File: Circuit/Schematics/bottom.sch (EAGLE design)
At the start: 42 parts, among them IC1 LM2936MP-3.3, X2 16 Mhz, X3 16 Mhz

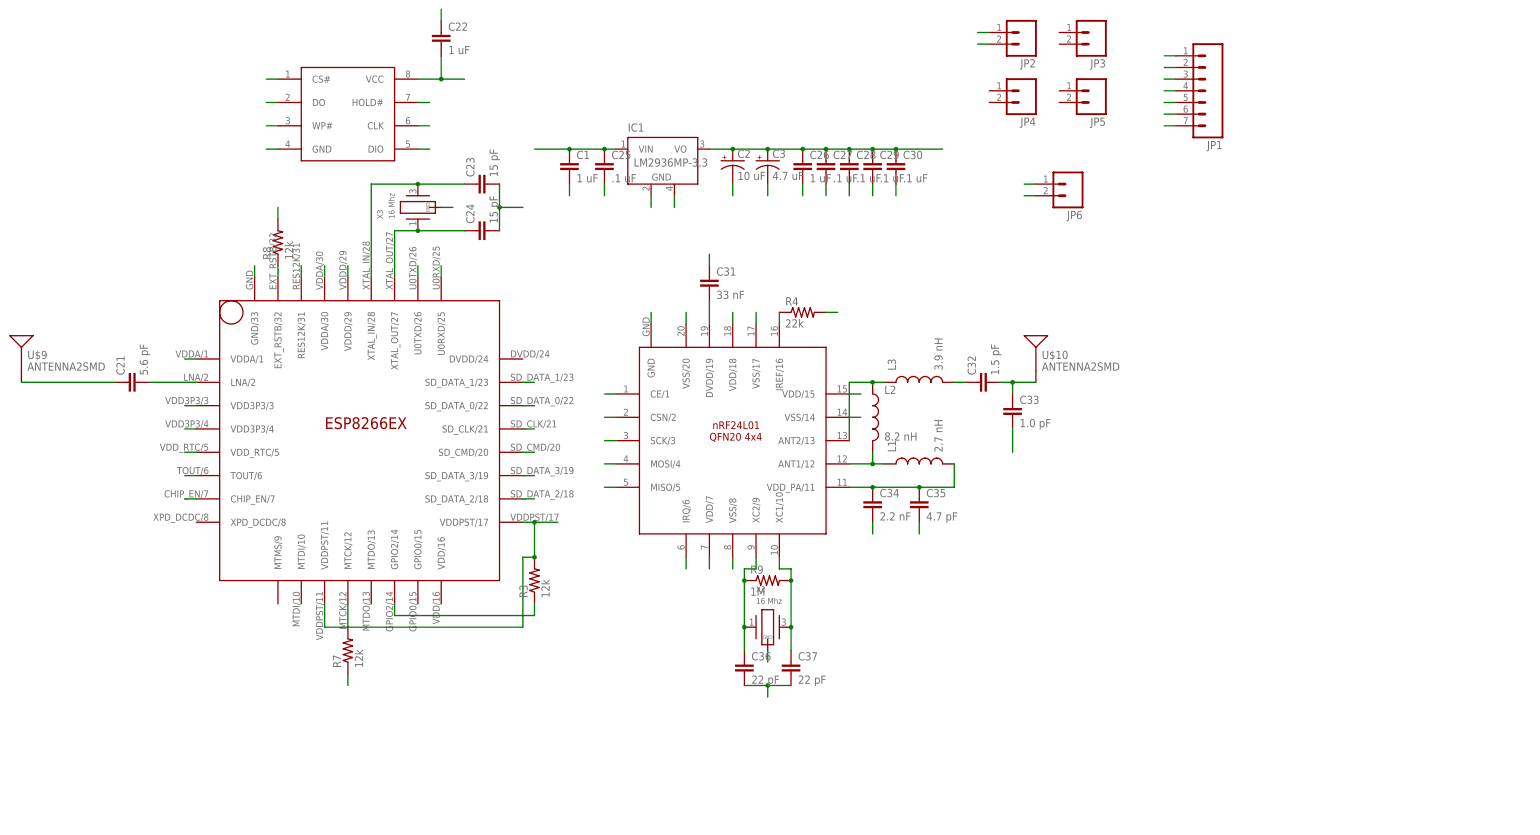
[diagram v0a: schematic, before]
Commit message: P1 preliminary boards finished
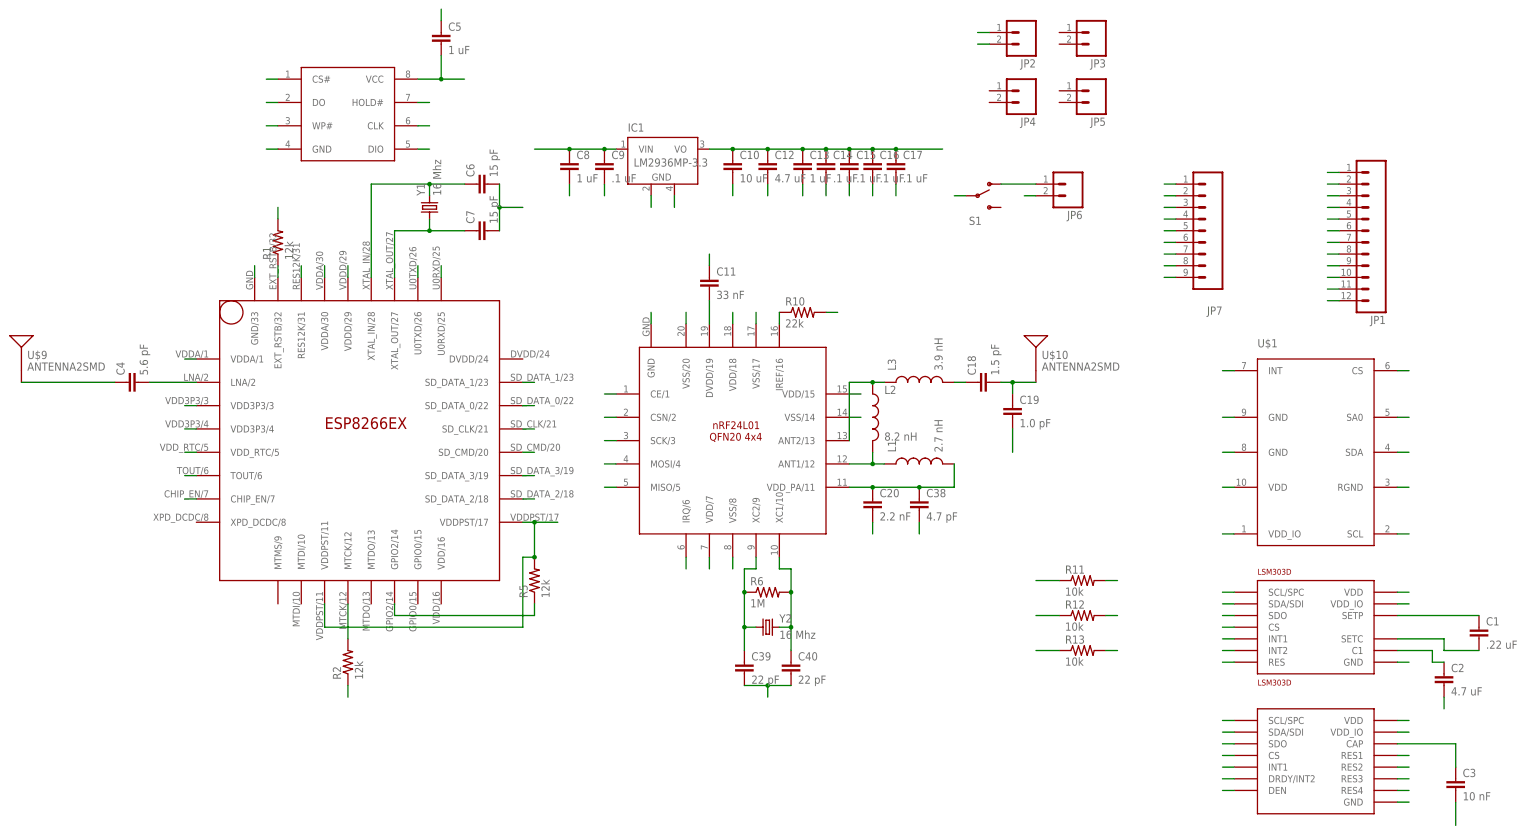
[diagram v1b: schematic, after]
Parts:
- removed C21: 5.6 pF, SparkFun-Capacitors:CAP0402-CAP
- removed C22, C26: 1 uF, SparkFun-Capacitors:CAP0402-CAP
- removed C23, C24: 15 pF, SparkFun-Capacitors:CAP0402-CAP
- removed C25, C27, C28, C29, C30: .1 uF, SparkFun-Capacitors:CAP0402-CAP
- removed C31: 33 nF, SparkFun-Capacitors:CAP0402-CAP
- removed C32: 1.5 pF, SparkFun-Capacitors:CAP0402-CAP
- removed C33: 1.0 pF, SparkFun-Capacitors:CAP0402-CAP
- removed C34: 2.2 nF, SparkFun-Capacitors:CAP0402-CAP
- removed C35: 4.7 pF, SparkFun-Capacitors:CAP0402-CAP
- removed C36, C37: 22 pF, SparkFun-Capacitors:CAP0402-CAP
- removed R3, R7, R8: 12k, SparkFun-Resistors:RESISTOR0402
- removed R4: 22k, SparkFun-Resistors:RESISTOR0402
- removed R9: 1M, SparkFun-Resistors:RESISTOR0402
- removed X2, X3: 16 Mhz, crystals:TXC-8Y
- added C10: 10 uF, SparkFun-Capacitors:CAP0603-CAP
- added C11: 33 nF, SparkFun-Capacitors:CAP0603-CAP
- added C12: 4.7 uF, SparkFun-Capacitors:CAP0603-CAP
- added C13, C5, C8: 1 uF, SparkFun-Capacitors:CAP0603-CAP
- added C14, C15, C16, C17, C9: .1 uF, SparkFun-Capacitors:CAP0603-CAP
- added C18: 1.5 pF, SparkFun-Capacitors:CAP0603-CAP
- added C19: 1.0 pF, SparkFun-Capacitors:CAP0603-CAP
- added C20: 2.2 nF, SparkFun-Capacitors:CAP0603-CAP
- added C38: 4.7 pF, SparkFun-Capacitors:CAP0603-CAP
- added C39, C40: 22 pF, SparkFun-Capacitors:CAP0603-CAP
- added C4: 5.6 pF, SparkFun-Capacitors:CAP0603-CAP
- added C6, C7: 15 pF, SparkFun-Capacitors:CAP0603-CAP
- added JP7: (no value), SparkFun-Connectors:M09
- added L3GD20H: L3GD20H, st:L3GD20H
- added LSM303D: LSM303D, st:LSM303D
- added R1, R2, R5: 12k, SparkFun-Resistors:RESISTOR0603-RES
- added R10: 22k, SparkFun-Resistors:RESISTOR0603-RES
- added R11, R12, R13: 10k, SparkFun-Resistors:RESISTOR0603-RES
- added R6: 1M, SparkFun-Resistors:RESISTOR0603-RES
- added S1: (no value), SparkFun-Electromechanical:SWITCH-SPDT-SMD-A
- added U$1: LPS25H, chips:LPS25H
- added Y1, Y2: 16 Mhz, SparkFun-FreqCtrl:CRYSTAL5X3
- C1: value 1 uF -> .22 uF; device SparkFun-Capacitors:CAP0402-CAP -> SparkFun-Capacitors:CAP0603-CAP
- C2: value 10 uF -> 4.7 uF; device SparkFun-Capacitors:CAP_POL1206 -> SparkFun-Capacitors:CAP0603-CAP
- C3: value 4.7 uF -> 10 nF; device SparkFun-Capacitors:CAP_POL1206 -> SparkFun-Capacitors:CAP0603-CAP
- JP1: device SparkFun-Connectors:M07 -> SparkFun-Connectors:M12PTH
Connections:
- removed net N$12: R7.2, WIFI.MTCK/12
- new net N$14: U$1.INT
- new net N$3: R2.2, WIFI.MTCK/12
- new net N$35: LSM303D.INT1
- new net N$36: LSM303D.INT2
- new net N$42: C1.2, LSM303D.SETC
- new net N$43: C2.1, LSM303D.C1
- new net N$49: L3GD20H.INT1
- new net N$50: L3GD20H.DRDY/INT2
- new net N$54: C3.1, L3GD20H.CAP
- new net SCL: JP7.9, L3GD20H.SCL/SPC, LSM303D.SCL/SPC, R12.2, U$1.SCL
- new net SDA: JP7.8, L3GD20H.SDA/SDI, LSM303D.SDA/SDI, R11.2, U$1.SDA
- new net SDO: L3GD20H.SDO, LSM303D.SDO, R13.2, U$1.SA0
- new net SETP: C1.1, LSM303D.SETP
- new net VIN: JP6.1, S1.O
- net CE: now also JP7.3; no longer JP1.3
- net CSN: now also JP7.4; no longer JP1.4
- net GND: now also C10.2, C11.1, C12.2, C13.2, C14.2, C15.2, C16.2, C17.2, C19.2, C2.2, C20.2, C3.2, C38.2, C39.2, C40.2, C5.1, C6.2, C7.2, C8.2, C9.2, JP1.1, JP1.2, JP1.3, JP1.4, JP1.5, JP1.6, L3GD20H.DEN, L3GD20H.GND, L3GD20H.RES1, L3GD20H.RES2, L3GD20H.RES3, LSM303D.GND, LSM303D.RES, R1.2, R10.2, R2.1, U$1.GND@1, U$1.GND@2, U$1.RGND; no longer C1.2, C2.-, C22.1, C23.2, C24.2, C25.2, C26.2, C27.2, C28.2, C29.2, C3.-, C30.2, C31.1, C33.2, C34.2, C35.2, C36.2, C37.2, R4.2, R7.1, R8.2, X2.GND, X3.GND
- net MISO: now also JP7.6; no longer JP1.6
- net MOSI: now also JP7.5; no longer JP1.5
- net N$1: now also C4.1; no longer C21.1
- net N$10: now also C18.2, C19.1; no longer C32.2, C33.1
- net N$13: now also C4.2; no longer C21.2
- net N$16: now also C39.1, R6.1, Y2.1; no longer C36.1, R9.1, X2.1
- net N$17: now also C40.1, R6.2, Y2.2; no longer C37.1, R9.2, X2.2
- net N$18: now also C20.1, C38.1; no longer C34.1, C35.1
- net N$2: now also R5.1; no longer R3.1
- net N$24: now also R10.1; no longer R4.1
- net N$28: now also C11.2; no longer C31.2
- net N$6: now also C18.1; no longer C32.1
- net RST: now also R1.1; no longer R8.1
- net RX_W: now also JP7.1; no longer JP1.1
- net SCK: now also JP7.7; no longer JP1.7
- net TX_W: now also JP7.2; no longer JP1.2
- net VDD: now also C10.1, C12.1, C13.1, C14.1, C15.1, C16.1, C17.1, C5.2, JP1.10, JP1.11, JP1.12, JP1.7, JP1.8, JP1.9, L3GD20H.CS, L3GD20H.RES4, L3GD20H.VDD, L3GD20H.VDD_IO, LSM303D.CS, LSM303D.VDD, LSM303D.VDD_IO, R11.1, R12.1, R13.1, R5.2, U$1.CS, U$1.VDD, U$1.VDD_IO; no longer C2.+, C22.2, C26.1, C27.1, C28.1, C29.1, C3.+, C30.1, R3.2
- net VRAW: now also C8.1, C9.1, S1.P; no longer C1.1, C25.1, JP6.1
- net XTAL_IN: now also C6.1, Y1.2; no longer C23.1, X3.2
- net XTAL_OUT: now also C7.1, Y1.1; no longer C24.1, X3.1
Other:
- moved on the sheet: C1
